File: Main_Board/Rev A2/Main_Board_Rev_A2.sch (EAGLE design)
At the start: 207 parts, among them J1 90814-0208, J12 22-27-2061-06, J15 1241050-5, J2 90814-0206, J3 90814-0208, J4 5504F1-09S-02A-03, J5 22-05-7048-04, J6 22-05-7048-04, J7 22-05-7058-05, J8 22-05-7048-04, J9 22-05-7028-02, K1 G6K-2G-Y, K2 G6K-2G-Y, K3 G6K-2G-Y, K4 G6K-2G-Y, P1 RB1-125BAG1A, SW1 B3FS-1050, SW2 B3FS-1050, T1 MMBT2222AL, U1 LT3686HDDPBF, U10 SN74LVC2G17DBVR, U11 MCP2561-E/SN, U12 TLV313, U2 TPL0401A, U3 SN74LVC3G17DCTR, U4 SN74LVC3G17DCTR, U5 LT3686HDDPBF, U6 LPC1768FBD100, U7 AT24C512C-SSHM-B, U8 SN74LVC3G17DCTR, U9 SN74LVC2G17DBVR, X1 ASE_50, X12 22-05-7028-02, X13 22-05-7028-02, X14 22-05-7038-03, X15 22-05-7038-03, X2 FC-135, X3 ASE-12, X4 MSTBA2, X5 22-05-7028-02, X6 USB3075-30-A, X7 3000, X8 22-05-7028-02

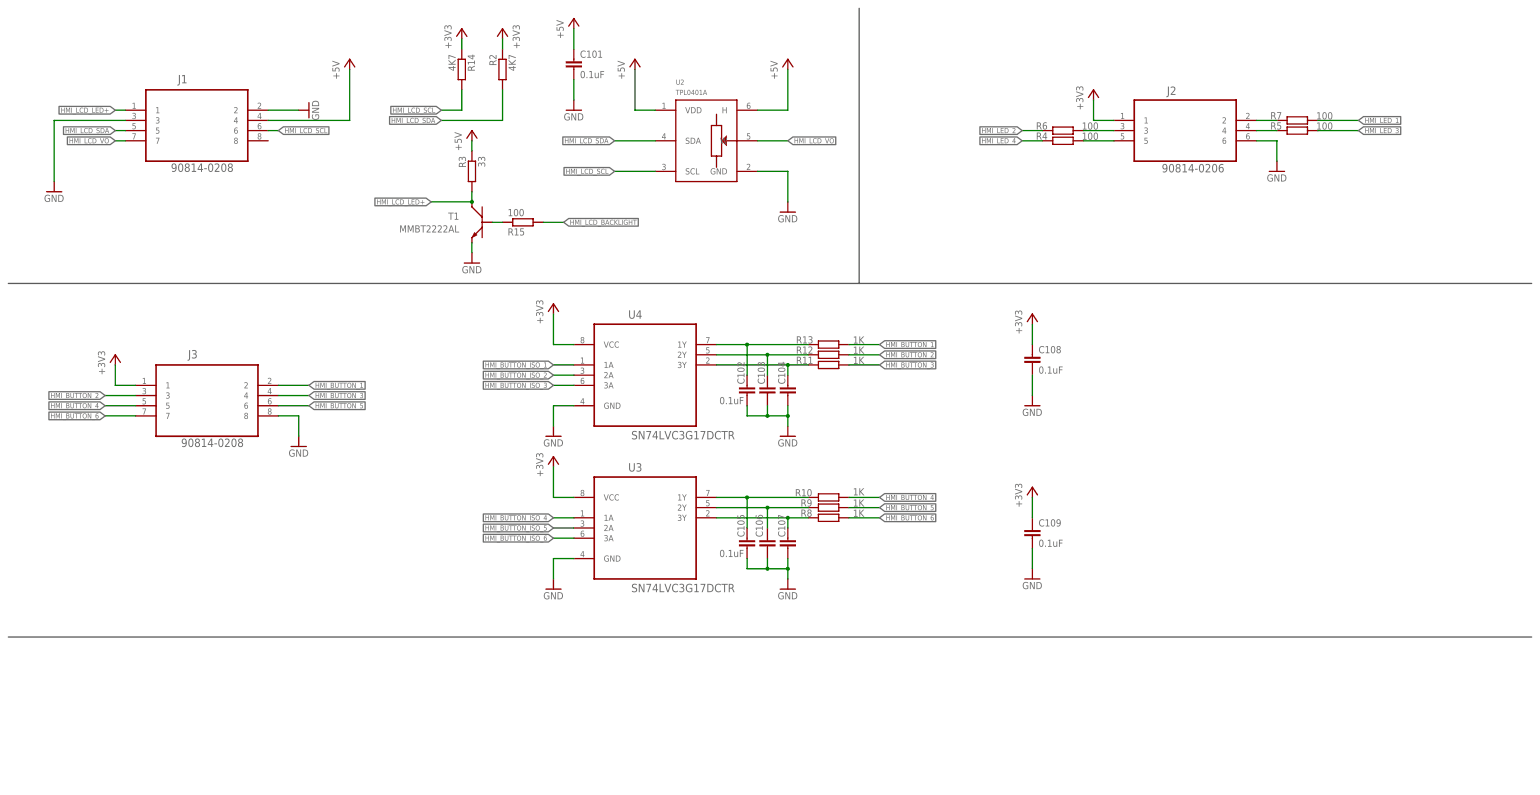
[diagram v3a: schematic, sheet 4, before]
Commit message: Repalce the HMI_LCD_LED+ npn interface into pnp interface
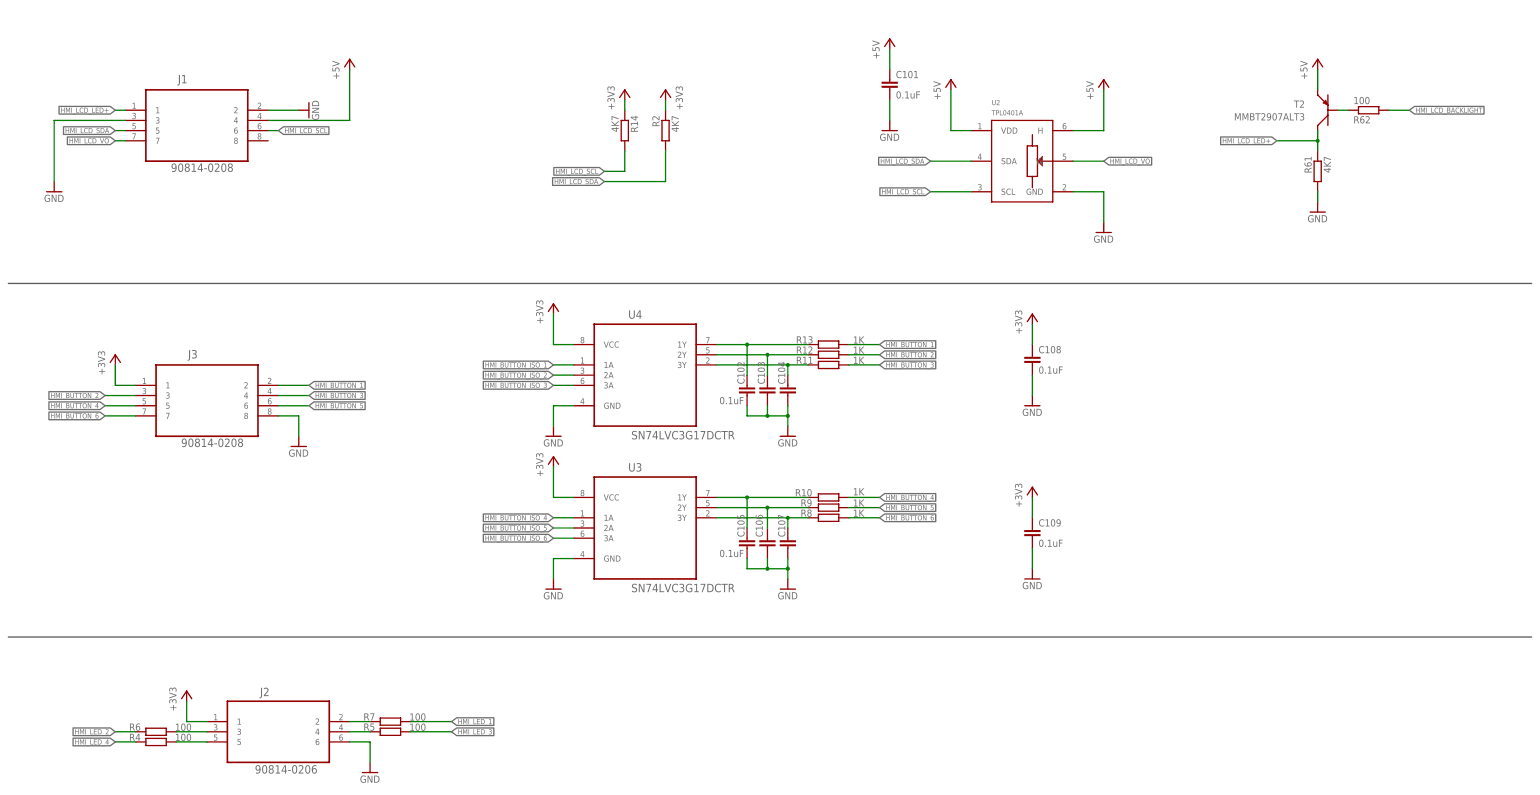
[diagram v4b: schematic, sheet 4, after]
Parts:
- removed R15: 100, rcl:R-EU_R0603
- removed R3: 33, rcl:R-EU_R0603
- removed T1: MMBT2222AL, transistor:MMBT2222AL
- added R61: 4K7, rcl:R-EU_R0603
- added R62: 100, rcl:R-EU_R0603
- added T2: MMBT2907ALT3, transistor:MMBT2907ALT3
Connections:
- removed net N$7: R15.1, T1.B
- new net N$67: R62.1, T2.B
- net +5V: now also T2.C; no longer R3.1
- net GND: now also R61.2; no longer T1.E
- net HMI_LCD_BACKLIGHT: now also R62.2; no longer R15.2
- net HMI_LCD_LED+: now also R61.1, T2.E; no longer R3.2, T1.C
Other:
- moved on the sheet: C101, J2, R14, R2, R4, R5, R6, R7, U2

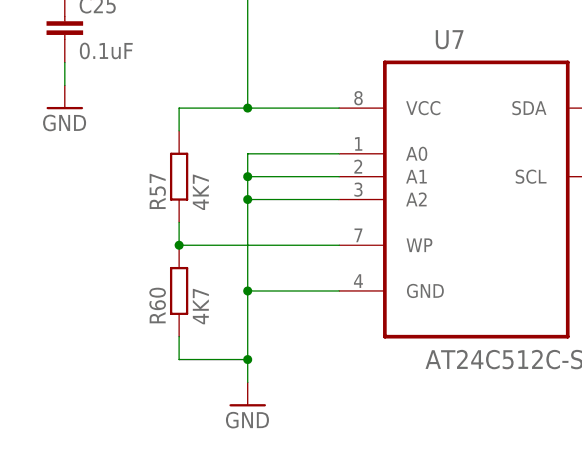
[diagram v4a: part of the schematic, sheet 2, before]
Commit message: 63 to 10k and add two test pad on EEPROM protection
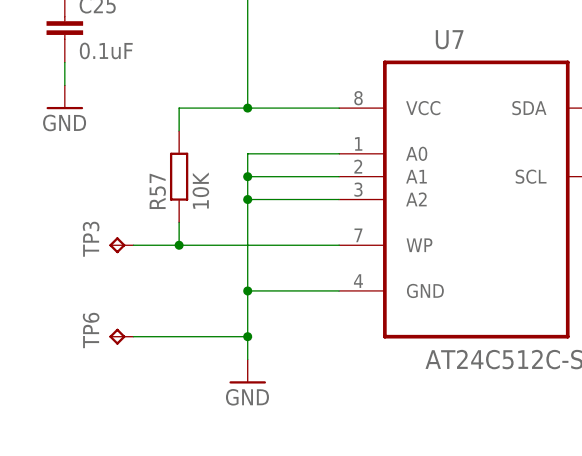
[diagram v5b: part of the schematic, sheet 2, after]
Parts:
- removed R60: 4K7, rcl:R-EU_R0603
- added TP3, TP6: TPB1,27, testpad:TPB1,27
- R57: value 4K7 -> 10K
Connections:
- net GND: now also TP6.TP; no longer R60.1
- net N$47: now also TP3.TP; no longer R60.2
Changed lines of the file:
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@@
 <part name="GND73" library="supply1" deviceset="GND" device=""/>
 <part name="+3V33" library="supply1" deviceset="+3V3" device=""/>
-<part name="R57" library="rcl" deviceset="R-EU_" device="R0603" value="4K7">
+<part name="R57" library="rcl" deviceset="R-EU_" device="R0603" value="10K">
 <attribute name="MF" value=""/>
 <attribute name="MPN" value="MCMR06X4701FTL"/>
@@
 <attribute name="OC_NEWARK" value="15R2205"/>
 </part>
-<part name="R60" library="rcl" deviceset="R-EU_" device="R0603" value="4K7">
-<attribute name="MF" value=""/>
-<attribute name="MPN" value="MCMR06X4701FTL"/>
-<attribute name="OC_NEWARK" value="86T3649"/>
-</part>
 <part name="J9" library="con-molex" deviceset="22-?-02" device="05-7028"/>
 <part name="GND87" library="supply1" deviceset="GND" device=""/>
@@
 <attribute name="OC_NEWARK" value="86T3504"/>
 </part>
+<part name="TP3" library="testpad" deviceset="TP" device="B1,27"/>
+<part name="TP6" library="testpad" deviceset="TP" device="B1,27"/>
 </parts>
 <sheets>
@@
 </instance>
 <instance part="+3V11" gate="G$1" x="33.02" y="58.42"/>
-<instance part="GND66" gate="1" x="33.02" y="5.08"/>
+<instance part="GND66" gate="1" x="33.02" y="7.62"/>
 <instance part="R17" gate="G$1" x="81.28" y="45.72" rot="R90">
 <attribute name="OC_NEWARK" x="81.28" y="45.72" size="1.778" layer="96" display="off"/>
@@
 </instance>
 <instance part="+3V14" gate="G$1" x="358.14" y="66.04"/>
-<instance part="R60" gate="G$1" x="25.4" y="17.78" rot="R90">
-<attribute name="OC_NEWARK" x="25.4" y="17.78" size="1.778" layer="96" display="off"/>
-<attribute name="MF" x="25.4" y="17.78" size="1.778" layer="96" display="off"/>
-<attribute name="MPN" x="25.4" y="17.78" size="1.778" layer="96" display="off"/>
-</instance>
+<instance part="TP3" gate="G$1" x="17.78" y="22.86" rot="R90"/>
+<instance part="TP6" gate="G$1" x="17.78" y="12.7" rot="R90"/>
 </instances>
 <busses>
@@
 <pinref part="GND66" gate="1" pin="GND"/>
 <wire x1="43.18" y1="17.78" x2="33.02" y2="17.78" width="0.1524" layer="91"/>
-<wire x1="33.02" y1="17.78" x2="33.02" y2="10.16" width="0.1524" layer="91"/>
+<wire x1="33.02" y1="17.78" x2="33.02" y2="12.7" width="0.1524" layer="91"/>
 <pinref part="U7" gate="A" pin="A0"/>
-<wire x1="33.02" y1="10.16" x2="33.02" y2="7.62" width="0.1524" layer="91"/>
+<wire x1="33.02" y1="12.7" x2="33.02" y2="10.16" width="0.1524" layer="91"/>
 <wire x1="43.18" y1="33.02" x2="33.02" y2="33.02" width="0.1524" layer="91"/>
 <wire x1="33.02" y1="33.02" x2="33.02" y2="30.48" width="0.1524" layer="91"/>
@@
 <wire x1="43.18" y1="27.94" x2="33.02" y2="27.94" width="0.1524" layer="91"/>
 <junction x="33.02" y="27.94"/>
-<junction x="33.02" y="10.16"/>
-<wire x1="25.4" y1="10.16" x2="33.02" y2="10.16" width="0.1524" layer="91"/>
-<pinref part="R60" gate="G$1" pin="1"/>
-<wire x1="25.4" y1="12.7" x2="25.4" y2="10.16" width="0.1524" layer="91"/>
+<junction x="33.02" y="12.7"/>
+<wire x1="20.32" y1="12.7" x2="33.02" y2="12.7" width="0.1524" layer="91"/>
+<pinref part="TP6" gate="G$1" pin="TP"/>
 </segment>
 <segment>
@@
 <wire x1="25.4" y1="25.4" x2="25.4" y2="22.86" width="0.1524" layer="91"/>
 <wire x1="25.4" y1="22.86" x2="43.18" y2="22.86" width="0.1524" layer="91"/>
-<pinref part="R60" gate="G$1" pin="2"/>
+<pinref part="TP3" gate="G$1" pin="TP"/>
+<wire x1="20.32" y1="22.86" x2="25.4" y2="22.86" width="0.1524" layer="91"/>
 <junction x="25.4" y="22.86"/>
 </segment>

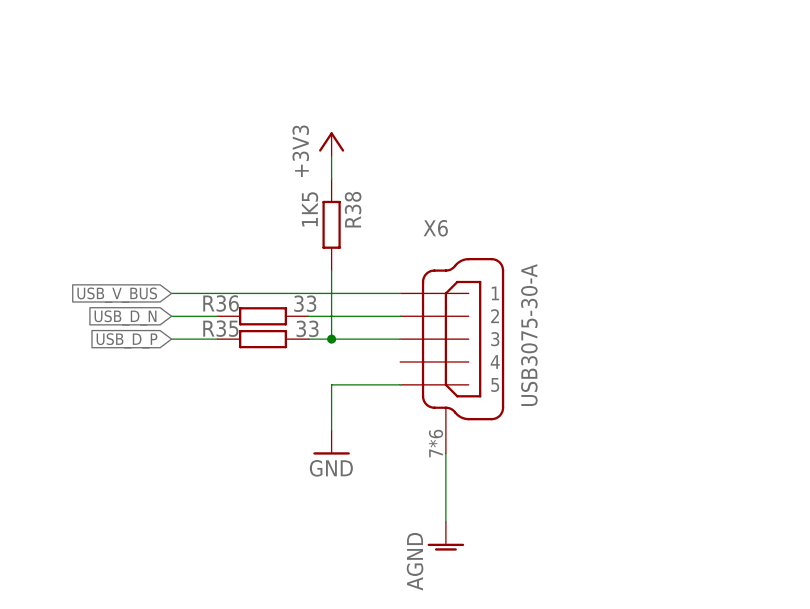
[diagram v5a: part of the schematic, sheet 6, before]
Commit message: add Pull-up resistor on USB_D_N for speed configuration
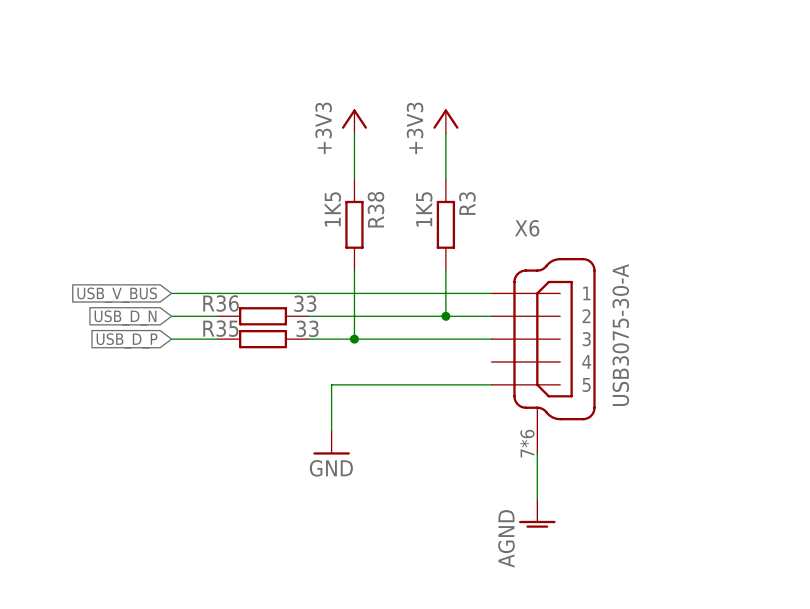
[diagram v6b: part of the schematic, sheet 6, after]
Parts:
- added R3: 1K5, rcl:R-EU_R0603
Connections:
- net +3V3: now also R3.1
- net N$15: now also R3.2
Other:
- moved on the sheet: R38, X6
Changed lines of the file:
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@@
 <part name="TP3" library="testpad" deviceset="TP" device="B1,27"/>
 <part name="TP6" library="testpad" deviceset="TP" device="B1,27"/>
+<part name="R3" library="rcl" deviceset="R-EU_" device="R0603" value="1K5">
+<attribute name="MF" value=""/>
+<attribute name="MPN" value="MCMR06X1501FTL"/>
+<attribute name="OC_NEWARK" value="86T3542"/>
+</part>
+<part name="+3V29" library="supply1" deviceset="+3V3" device=""/>
 </parts>
 <sheets>
@@
 <instance part="J12" gate="-6" x="35.56" y="200.66" rot="MR0"/>
 <instance part="GND89" gate="1" x="42.418" y="194.818"/>
-<instance part="X6" gate="J$1" x="167.64" y="213.36">
-<attribute name="OC_NEWARK" x="167.64" y="213.36" size="1.778" layer="96" display="off"/>
-<attribute name="MF" x="167.64" y="213.36" size="1.778" layer="96" display="off"/>
-<attribute name="MPN" x="167.64" y="213.36" size="1.778" layer="96" display="off"/>
+<instance part="X6" gate="J$1" x="177.8" y="213.36">
+<attribute name="OC_NEWARK" x="177.8" y="213.36" size="1.778" layer="96" display="off"/>
+<attribute name="MF" x="177.8" y="213.36" size="1.778" layer="96" display="off"/>
+<attribute name="MPN" x="177.8" y="213.36" size="1.778" layer="96" display="off"/>
 </instance>
 <instance part="R36" gate="G$1" x="147.32" y="215.9" smashed="yes" rot="R180">
@@
 </instance>
 <instance part="GND27" gate="1" x="154.94" y="200.66"/>
-<instance part="R38" gate="G$1" x="154.94" y="226.06" rot="R270">
-<attribute name="OC_NEWARK" x="154.94" y="226.06" size="1.778" layer="96" display="off"/>
-<attribute name="MF" x="154.94" y="226.06" size="1.778" layer="96" display="off"/>
-<attribute name="MPN" x="154.94" y="226.06" size="1.778" layer="96" display="off"/>
+<instance part="R38" gate="G$1" x="157.48" y="226.06" rot="R270">
+<attribute name="OC_NEWARK" x="157.48" y="226.06" size="1.778" layer="96" display="off"/>
+<attribute name="MF" x="157.48" y="226.06" size="1.778" layer="96" display="off"/>
+<attribute name="MPN" x="157.48" y="226.06" size="1.778" layer="96" display="off"/>
 </instance>
-<instance part="+3V17" gate="G$1" x="154.94" y="236.22"/>
+<instance part="+3V17" gate="G$1" x="157.48" y="238.76"/>
 <instance part="LED5" gate="G$1" x="106.68" y="226.06">
 <attribute name="OC_NEWARK" x="106.68" y="226.06" size="1.778" layer="96" display="off"/>
@@
 <instance part="+3V324" gate="G$1" x="312.42" y="233.68"/>
 <instance part="GND90" gate="1" x="312.42" y="190.5"/>
-<instance part="AGND3" gate="VR1" x="167.64" y="190.5"/>
+<instance part="AGND3" gate="VR1" x="177.8" y="193.04"/>
+<instance part="R3" gate="G$1" x="167.64" y="226.06" rot="R270">
+<attribute name="OC_NEWARK" x="167.64" y="226.06" size="1.778" layer="96" display="off"/>
+<attribute name="MF" x="167.64" y="226.06" size="1.778" layer="96" display="off"/>
+<attribute name="MPN" x="167.64" y="226.06" size="1.778" layer="96" display="off"/>
+</instance>
+<instance part="+3V29" gate="G$1" x="167.64" y="238.76"/>
 </instances>
 <busses>
@@
 <pinref part="X6" gate="J$1" pin="5"/>
 <pinref part="GND27" gate="1" pin="GND"/>
-<wire x1="162.56" y1="208.28" x2="154.94" y2="208.28" width="0.1524" layer="91"/>
+<wire x1="172.72" y1="208.28" x2="154.94" y2="208.28" width="0.1524" layer="91"/>
 <wire x1="154.94" y1="208.28" x2="154.94" y2="203.2" width="0.1524" layer="91"/>
 </segment>
@@
 <net name="+3V3" class="2">
 <segment>
-<pinref part="R38" gate="G$1" pin="1"/>
 <pinref part="+3V17" gate="G$1" pin="+3V3"/>
-<wire x1="154.94" y1="231.14" x2="154.94" y2="233.68" width="0.1524" layer="91"/>
+<pinref part="R38" gate="G$1" pin="1"/>
+<wire x1="157.48" y1="231.14" x2="157.48" y2="236.22" width="0.1524" layer="91"/>
+</segment>
+<segment>
+<pinref part="R3" gate="G$1" pin="1"/>
+<pinref part="+3V29" gate="G$1" pin="+3V3"/>
+<wire x1="167.64" y1="231.14" x2="167.64" y2="236.22" width="0.1524" layer="91"/>
 </segment>
 <segment>
@@
 <pinref part="R36" gate="G$1" pin="1"/>
 <pinref part="X6" gate="J$1" pin="2"/>
-<wire x1="152.4" y1="215.9" x2="162.56" y2="215.9" width="0.1524" layer="91"/>
+<wire x1="152.4" y1="215.9" x2="167.64" y2="215.9" width="0.1524" layer="91"/>
+<pinref part="R3" gate="G$1" pin="2"/>
+<wire x1="167.64" y1="215.9" x2="172.72" y2="215.9" width="0.1524" layer="91"/>
+<wire x1="167.64" y1="215.9" x2="167.64" y2="220.98" width="0.1524" layer="91"/>
+<junction x="167.64" y="215.9"/>
 </segment>
 </net>
@@
 <pinref part="R35" gate="G$1" pin="1"/>
 <pinref part="X6" gate="J$1" pin="3"/>
-<wire x1="152.4" y1="213.36" x2="154.94" y2="213.36" width="0.1524" layer="91"/>
+<wire x1="152.4" y1="213.36" x2="157.48" y2="213.36" width="0.1524" layer="91"/>
 <pinref part="R38" gate="G$1" pin="2"/>
-<wire x1="154.94" y1="213.36" x2="162.56" y2="213.36" width="0.1524" layer="91"/>
-<wire x1="154.94" y1="220.98" x2="154.94" y2="213.36" width="0.1524" layer="91"/>
-<junction x="154.94" y="213.36"/>
+<wire x1="157.48" y1="213.36" x2="172.72" y2="213.36" width="0.1524" layer="91"/>
+<wire x1="157.48" y1="220.98" x2="157.48" y2="213.36" width="0.1524" layer="91"/>
+<junction x="157.48" y="213.36"/>
 </segment>
 </net>
@@
 <segment>
 <pinref part="X6" gate="J$1" pin="1"/>
-<wire x1="162.56" y1="218.44" x2="137.16" y2="218.44" width="0.1524" layer="91"/>
+<wire x1="172.72" y1="218.44" x2="137.16" y2="218.44" width="0.1524" layer="91"/>
 <label x="137.16" y="218.44" size="1.27" layer="95" rot="R180" xref="yes"/>
 </segment>
@@
 <pinref part="X6" gate="J$1" pin="S"/>
 <pinref part="AGND3" gate="VR1" pin="AGND"/>
-<wire x1="167.64" y1="200.66" x2="167.64" y2="193.04" width="0.1524" layer="91"/>
+<wire x1="177.8" y1="200.66" x2="177.8" y2="195.58" width="0.1524" layer="91"/>
 </segment>
 </net>

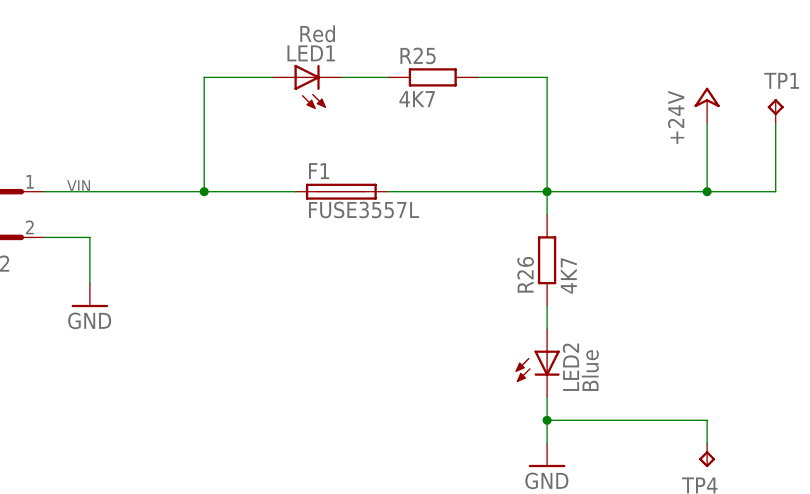
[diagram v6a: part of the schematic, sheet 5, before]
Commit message: Repalce Fuse by polyfuse
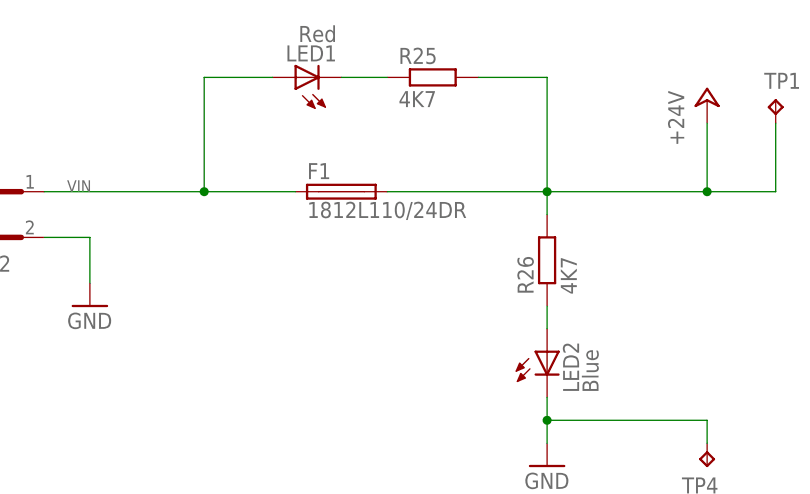
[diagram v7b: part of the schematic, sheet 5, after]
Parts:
- F1: value FUSE3557L -> 1812L110/24DR; device fuse2:FUSE3557L -> fuse2:1812L110/24DR
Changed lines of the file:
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@@
 <part name="FRAME5" library="frames" deviceset="A3L-LOC" device=""/>
 <part name="X4" library="con-phoenix-508" deviceset="MSTBA2" device=""/>
-<part name="F1" library="fuse2" deviceset="FUSE" device="3557L">
+<part name="F1" library="fuse2" deviceset="1812L" device="" technology="110/24DR" value="1812L110/24DR">
 <attribute name="MF" value=""/>
 <attribute name="MPN" value="3557"/>
